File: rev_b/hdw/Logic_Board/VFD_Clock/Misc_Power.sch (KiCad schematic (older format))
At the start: 16 parts, among them Q1301 BSS214NW, Q1302 ZXMS6004FFTA, Q1304 BSS214NW, Q1306 ZXMS6004FFTA, Q1307 BSS214NW, Q1308 ZXMS6004FFTA

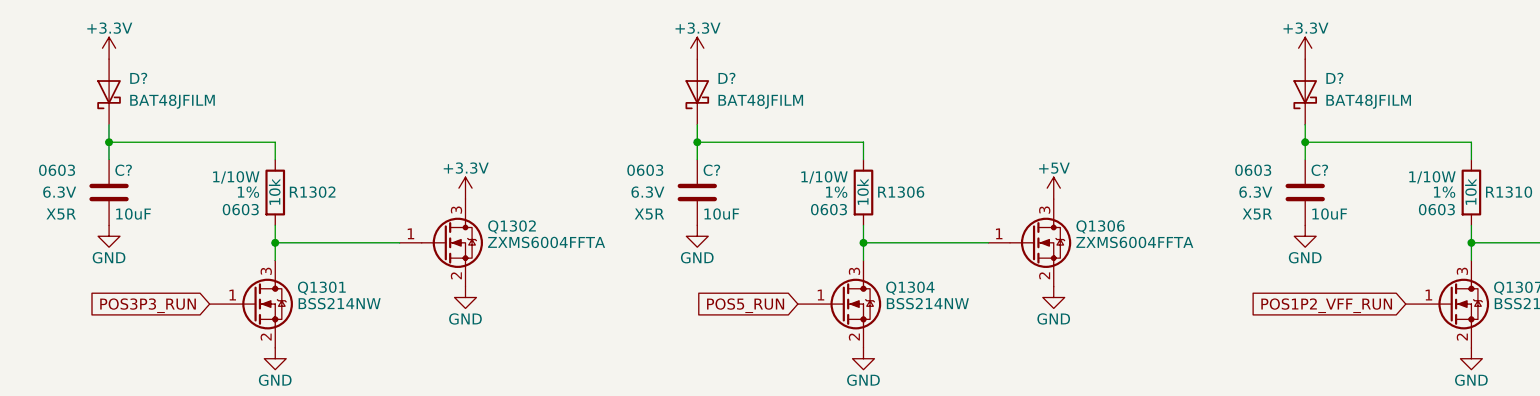
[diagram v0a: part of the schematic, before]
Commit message: PCB changes, deletions
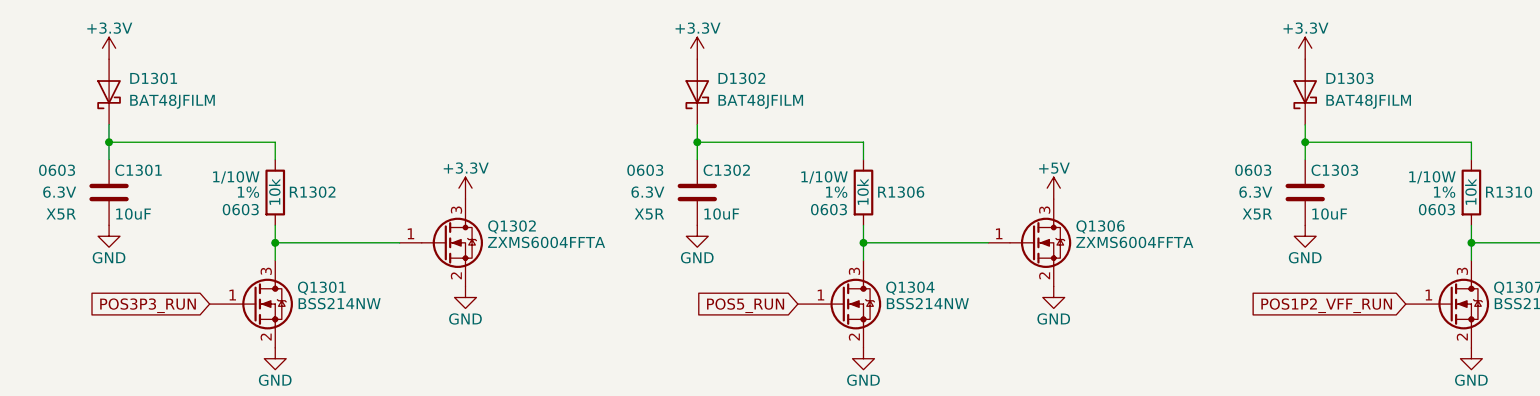
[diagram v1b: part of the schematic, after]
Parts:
- gave numbers to parts that had none: 6
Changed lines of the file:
@@
 AR Path="/5A557C58/5F9449C3" Ref="C?"  Part="1"
 AR Path="/5CB25152/5F9449C3" Ref="C?"  Part="1"
-AR Path="/5E1352F5/5F9449C3" Ref="C?"  Part="1"
-F 0 "C?" H 2075 1950 50  0000 L CNN
+AR Path="/5E1352F5/5F9449C3" Ref="C1301"  Part="1"
+F 0 "C1301" H 2075 1950 50  0000 L CNN
 F 1 "10uF" H 2075 1750 50  0000 L CNN
 F 2 "Capacitors_SMD:C_0603" H 2088 1700 50  0001 C CNN
@@
 P 2050 2000
 AR Path="/5CB0BC26/5F944AE4" Ref="#PWR?"  Part="1"
-AR Path="/5E1352F5/5F944AE4" Ref="#PWR?"  Part="1"
-F 0 "#PWR?" H 2050 1750 50  0001 C CNN
+AR Path="/5E1352F5/5F944AE4" Ref="#PWR01305"  Part="1"
+F 0 "#PWR01305" H 2050 1750 50  0001 C CNN
 F 1 "GND" H 2050 1850 50  0000 C CNN
 F 2 "" H 2050 2000 50  0001 C CNN
@@
 P 2050 1390
 AR Path="/5E07B870/5F94DC32" Ref="D?"  Part="1"
-AR Path="/5E1352F5/5F94DC32" Ref="D?"  Part="1"
-F 0 "D?" V 2110 1300 50  0000 R CNN
+AR Path="/5E1352F5/5F94DC32" Ref="D1301"  Part="1"
+F 0 "D1301" V 2110 1300 50  0000 R CNN
 F 1 "BAT48JFILM" V 2010 1300 50  0000 R CNN
 F 2 "Diode_SMD:D_SOD-323" H 2050 1215 50  0001 C CNN
@@
 Connection ~ 2050 1620
 $Comp
-L power:+3.3V #PWR?
+L power:+3.3V #PWR01301
 U 1 1 5F94E116
 P 2050 1240
-F 0 "#PWR?" H 2050 1090 50  0001 C CNN
+F 0 "#PWR01301" H 2050 1090 50  0001 C CNN
 F 1 "+3.3V" H 2050 1380 50  0000 C CNN
 F 2 "" H 2050 1240 50  0001 C CNN
@@
 AR Path="/5A557C58/5F94EFEF" Ref="C?"  Part="1"
 AR Path="/5CB25152/5F94EFEF" Ref="C?"  Part="1"
-AR Path="/5E1352F5/5F94EFEF" Ref="C?"  Part="1"
-F 0 "C?" H 4765 1950 50  0000 L CNN
+AR Path="/5E1352F5/5F94EFEF" Ref="C1302"  Part="1"
+F 0 "C1302" H 4765 1950 50  0000 L CNN
 F 1 "10uF" H 4765 1750 50  0000 L CNN
 F 2 "Capacitors_SMD:C_0603" H 4778 1700 50  0001 C CNN
@@
 P 4740 2000
 AR Path="/5CB0BC26/5F94EFF9" Ref="#PWR?"  Part="1"
-AR Path="/5E1352F5/5F94EFF9" Ref="#PWR?"  Part="1"
-F 0 "#PWR?" H 4740 1750 50  0001 C CNN
+AR Path="/5E1352F5/5F94EFF9" Ref="#PWR01307"  Part="1"
+F 0 "#PWR01307" H 4740 1750 50  0001 C CNN
 F 1 "GND" H 4740 1850 50  0000 C CNN
 F 2 "" H 4740 2000 50  0001 C CNN
@@
 P 4740 1390
 AR Path="/5E07B870/5F94F005" Ref="D?"  Part="1"
-AR Path="/5E1352F5/5F94F005" Ref="D?"  Part="1"
-F 0 "D?" V 4800 1300 50  0000 R CNN
+AR Path="/5E1352F5/5F94F005" Ref="D1302"  Part="1"
+F 0 "D1302" V 4800 1300 50  0000 R CNN
 F 1 "BAT48JFILM" V 4700 1300 50  0000 R CNN
 F 2 "Diode_SMD:D_SOD-323" H 4740 1215 50  0001 C CNN
@@
 Connection ~ 4740 1620
 $Comp
-L power:+3.3V #PWR?
+L power:+3.3V #PWR01306
 U 1 1 5F94F011
 P 4740 1240
-F 0 "#PWR?" H 4740 1090 50  0001 C CNN
+F 0 "#PWR01306" H 4740 1090 50  0001 C CNN
 F 1 "+3.3V" H 4740 1380 50  0000 C CNN
 F 2 "" H 4740 1240 50  0001 C CNN
@@
 AR Path="/5A557C58/5F95480C" Ref="C?"  Part="1"
 AR Path="/5CB25152/5F95480C" Ref="C?"  Part="1"
-AR Path="/5E1352F5/5F95480C" Ref="C?"  Part="1"
-F 0 "C?" H 7545 1950 50  0000 L CNN
+AR Path="/5E1352F5/5F95480C" Ref="C1303"  Part="1"
+F 0 "C1303" H 7545 1950 50  0000 L CNN
 F 1 "10uF" H 7545 1750 50  0000 L CNN
 F 2 "Capacitors_SMD:C_0603" H 7558 1700 50  0001 C CNN
@@
 P 7520 2000
 AR Path="/5CB0BC26/5F954816" Ref="#PWR?"  Part="1"
-AR Path="/5E1352F5/5F954816" Ref="#PWR?"  Part="1"
-F 0 "#PWR?" H 7520 1750 50  0001 C CNN
+AR Path="/5E1352F5/5F954816" Ref="#PWR01310"  Part="1"
+F 0 "#PWR01310" H 7520 1750 50  0001 C CNN
 F 1 "GND" H 7520 1850 50  0000 C CNN
 F 2 "" H 7520 2000 50  0001 C CNN
@@
 P 7520 1390
 AR Path="/5E07B870/5F954822" Ref="D?"  Part="1"
-AR Path="/5E1352F5/5F954822" Ref="D?"  Part="1"
-F 0 "D?" V 7580 1300 50  0000 R CNN
+AR Path="/5E1352F5/5F954822" Ref="D1303"  Part="1"
+F 0 "D1303" V 7580 1300 50  0000 R CNN
 F 1 "BAT48JFILM" V 7480 1300 50  0000 R CNN
 F 2 "Diode_SMD:D_SOD-323" H 7520 1215 50  0001 C CNN
@@
 Connection ~ 7520 1620
 $Comp
-L power:+3.3V #PWR?
+L power:+3.3V #PWR01308
 U 1 1 5F95482E
 P 7520 1240
-F 0 "#PWR?" H 7520 1090 50  0001 C CNN
+F 0 "#PWR01308" H 7520 1090 50  0001 C CNN
 F 1 "+3.3V" H 7520 1380 50  0000 C CNN
 F 2 "" H 7520 1240 50  0001 C CNN
